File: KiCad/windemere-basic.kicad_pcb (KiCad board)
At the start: 2 copper layers, 146.1 x 157.5 mm, 57 parts, among them J1 Barrel_Jack, SW1 Push_Button, SW2 SW_SPDT, U1 HD44780U, U2 WD65C02, U3 28C256, U4 62256, U5 WD65C22, U6 74HC00, U7 MM74C922, U8 L7805, X1 1MHz

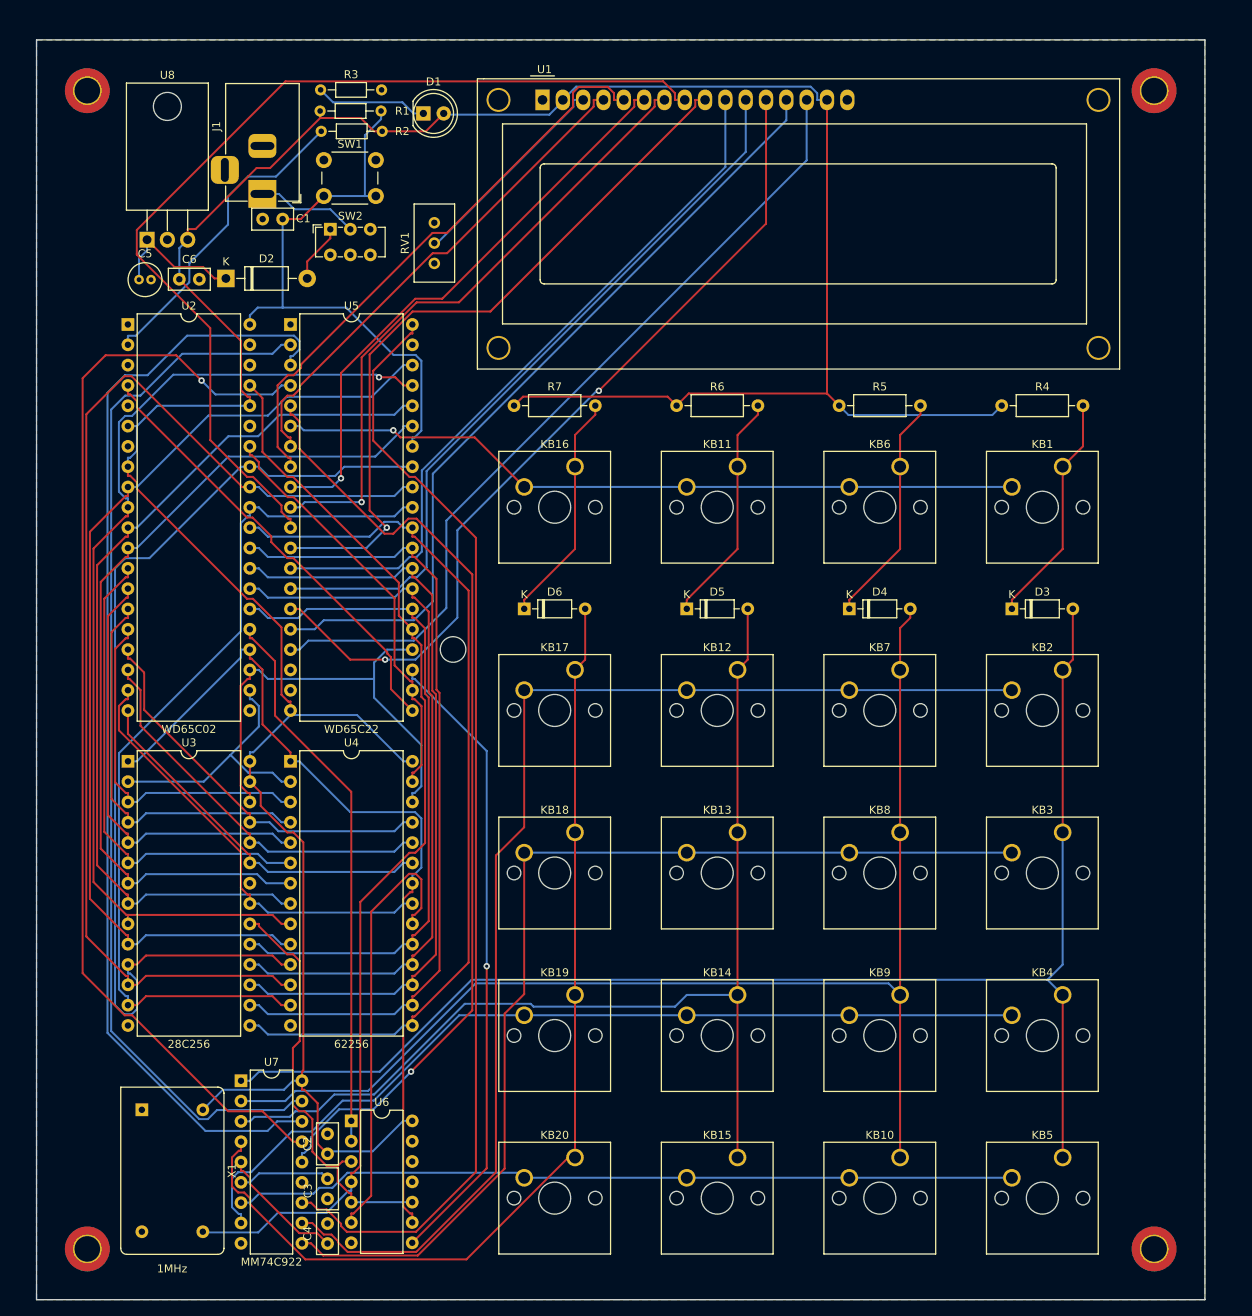
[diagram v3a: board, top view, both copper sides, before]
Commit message: Add J1
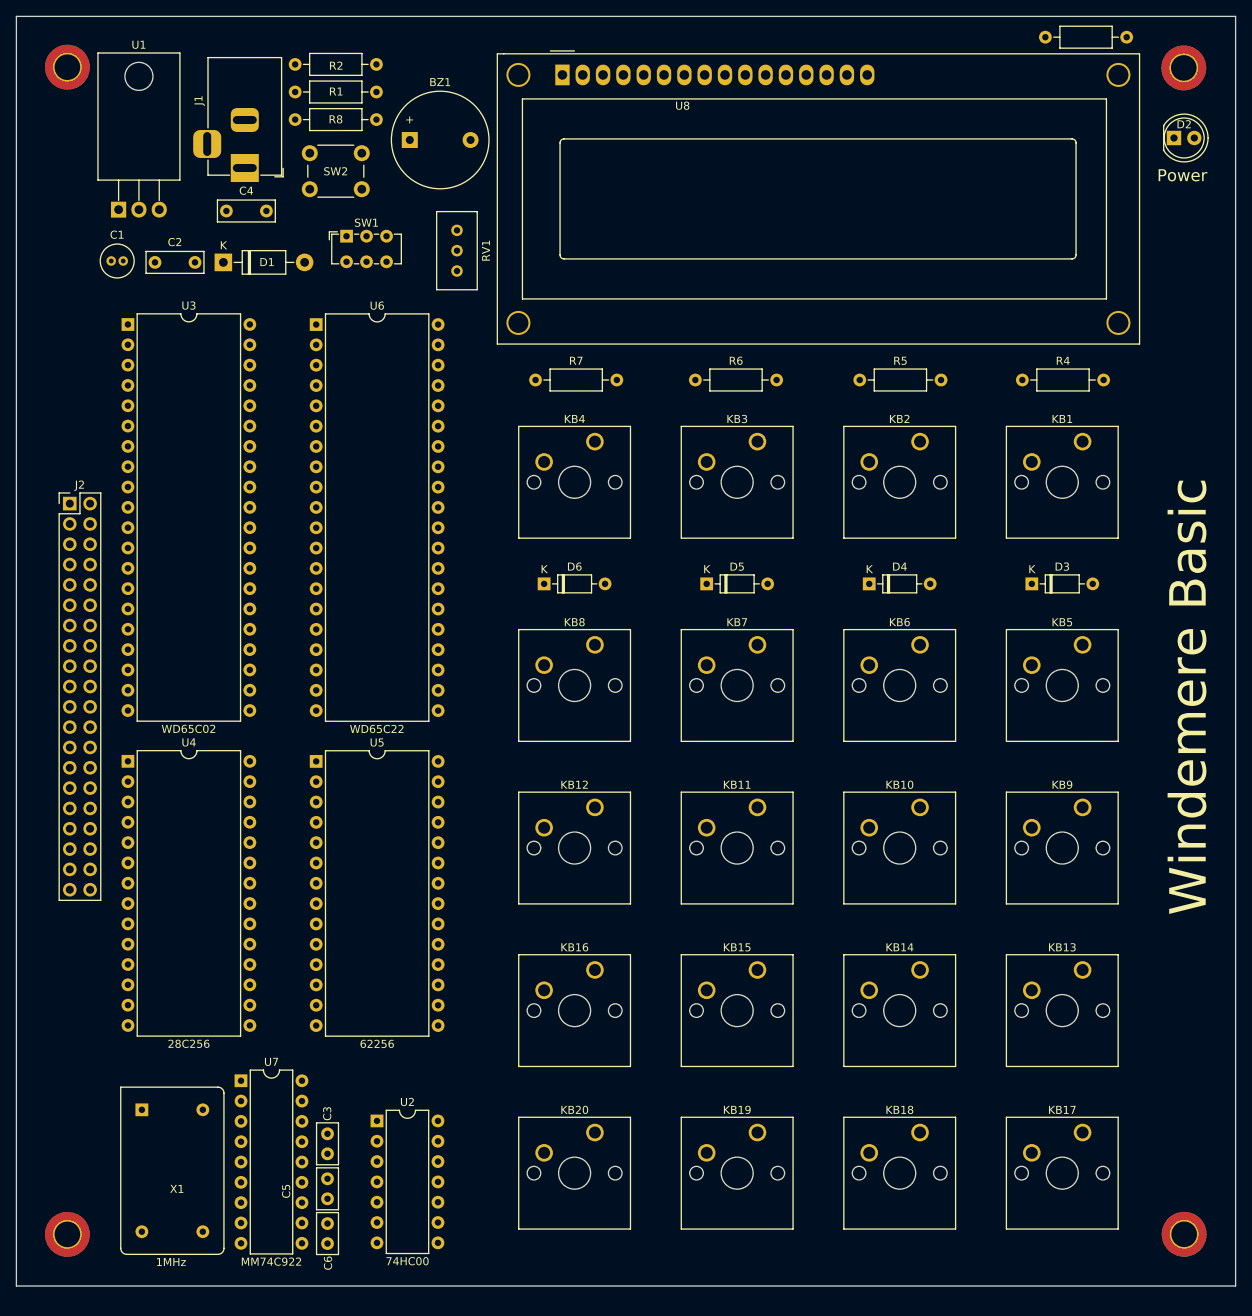
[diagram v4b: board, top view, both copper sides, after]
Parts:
- removed the R7 at (195.6, 81.3)
- removed REF?: MountingHole_3.2mm_M3, MountingHole:MountingHole_3.2mm_M3
- removed the U1 at (199.1, 43.1)
- added BZ1: Buzzer, Buzzer_Beeper:Buzzer_12x9.5RM7.6, F.Cu at (182.6, 48.1)
- added J2: Conn_02x20, Connector_PinHeader_2.54mm:PinHeader_2x20_P2.54mm_Vertical, F.Cu at (140.1, 93.5)
- added R3: 1k, Resistor_THT:R_Axial_DIN0207_L6.3mm_D2.5mm_P10.16mm_Horizontal, F.Cu at (262.0, 35.2)
- added R8: 1K, Resistor_THT:R_Axial_DIN0207_L6.3mm_D2.5mm_P10.16mm_Horizontal, F.Cu at (168.2, 45.5)
- added REF**: OSHW-Logo_11.4x12mm_SilkScreen, Symbol:OSHW-Logo_11.4x12mm_SilkScreen, B.Cu at (208.0, 65.2)
- added U8: HD44780U, Display:WC1602A, F.Cu at (201.6, 39.9)
- added memory_map: 6502-Memory_Map, memory_map:6502-Memory_Map, F.Cu at (236.0, 65.3)
- C2: renamed from C6; footprint Capacitor_THT:C_Disc_D5.0mm_W2.5mm_P2.50mm -> Capacitor_THT:C_Disc_D7.0mm_W2.5mm_P5.00mm
- C4: renamed from C1; footprint Capacitor_THT:C_Disc_D5.0mm_W2.5mm_P2.50mm -> Capacitor_THT:C_Disc_D7.0mm_W2.5mm_P5.00mm
- R1: renamed from R2; footprint Resistor_THT:R_Axial_DIN0204_L3.6mm_D1.6mm_P7.62mm_Horizontal -> Resistor_THT:R_Axial_DIN0207_L6.3mm_D2.5mm_P10.16mm_Horizontal
- R2: renamed from R3; value 1k -> 1K; footprint Resistor_THT:R_Axial_DIN0204_L3.6mm_D1.6mm_P7.62mm_Horizontal -> Resistor_THT:R_Axial_DIN0207_L6.3mm_D2.5mm_P10.16mm_Horizontal
- R7: renamed from R1; value 1K -> 100K; footprint Resistor_THT:R_Axial_DIN0204_L3.6mm_D1.6mm_P7.62mm_Horizontal -> Resistor_THT:R_Axial_DIN0207_L6.3mm_D2.5mm_P10.16mm_Horizontal
- SW2: renamed from SW1; value Push_Button -> Push_Button_small
- moved D2 93.9 mm to (278.1, 47.8)
- moved KB4 90.6 mm to (205.7, 85.8)
- moved KB17 85.9 mm to (266.6, 172.1)
- moved KB5 64.1 mm to (266.6, 111.2)
- moved KB16 63.0 mm to (205.7, 151.8)
- moved KB3 62.0 mm to (226.0, 85.8)
- moved KB18 57.2 mm to (246.3, 172.1)
- moved KB13 46.4 mm to (266.6, 151.8)
- moved KB8 44.8 mm to (205.7, 111.2)
- moved KB10 43.8 mm to (246.3, 131.5)
- moved R7 43.1 mm to (198.3, 78.1)
- moved KB11 42.7 mm to (226.0, 131.5)
- moved KB2 33.6 mm to (246.3, 85.8)
- moved KB9 32.7 mm to (266.6, 131.5)
- moved KB19 28.6 mm to (226.0, 172.1)
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- renumbered C5 to C1, C2 to C3, C3 to C5, C4 to C6, D2 to D1, D1 to D2, SW2 to SW1, U8 to U1, U6 to U2, U2 to U3, U3 to U4, U4 to U5, U5 to U6
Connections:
- C4 pad 1: Net-(C1-Pad1) (its old number) -> Net-(C4-Pad1)
- D2 pad 1: Net-(D1-Pad1) -> Net-(D2-Pad1)
- KB11 pad 1: Net-(D5-Pad1) -> Net-(D5-Pad2)
- KB11 pad 2: Net-(KB1-Pad2) -> Net-(KB10-Pad2)
- KB12 pad 1: Net-(D5-Pad2) -> Net-(D6-Pad2)
- KB12 pad 2: Net-(KB12-Pad2) -> Net-(KB10-Pad2)
- KB13 pad 1: Net-(D5-Pad2) -> Net-(D3-Pad2)
- KB14 pad 1: Net-(D5-Pad2) -> Net-(D4-Pad2)
- KB14 pad 2: Net-(KB14-Pad2) -> Net-(KB13-Pad2)
- KB15 pad 2: Net-(KB10-Pad2) -> Net-(KB13-Pad2)
- KB16 pad 1: Net-(D6-Pad1) -> Net-(D6-Pad2)
- KB16 pad 2: Net-(KB1-Pad2) -> Net-(KB13-Pad2)
- KB17 pad 1: Net-(D6-Pad2) -> Net-(D3-Pad2)
- KB17 pad 2: Net-(KB12-Pad2) -> Net-(KB17-Pad2)
- KB18 pad 1: Net-(D6-Pad2) -> Net-(D4-Pad2)
- KB18 pad 2: Net-(KB13-Pad2) -> Net-(KB17-Pad2)
- KB19 pad 1: Net-(D6-Pad2) -> Net-(D5-Pad2)
- KB19 pad 2: Net-(KB14-Pad2) -> Net-(KB17-Pad2)
- KB2 pad 1: Net-(D3-Pad2) -> Net-(D4-Pad1)
- KB2 pad 2: Net-(KB12-Pad2) -> Net-(KB1-Pad2)
- KB20 pad 2: Net-(KB10-Pad2) -> Net-(KB17-Pad2)
- KB3 pad 1: Net-(D3-Pad2) -> Net-(D5-Pad1)
- KB3 pad 2: Net-(KB13-Pad2) -> Net-(KB1-Pad2)
- KB4 pad 1: Net-(D3-Pad2) -> Net-(D6-Pad1)
- KB4 pad 2: Net-(KB14-Pad2) -> Net-(KB1-Pad2)
- KB5 pad 2: Net-(KB10-Pad2) -> Net-(KB5-Pad2)
- KB6 pad 1: Net-(D4-Pad1) -> Net-(D4-Pad2)
- KB6 pad 2: Net-(KB1-Pad2) -> Net-(KB5-Pad2)
- KB7 pad 1: Net-(D4-Pad2) -> Net-(D5-Pad2)
- KB7 pad 2: Net-(KB12-Pad2) -> Net-(KB5-Pad2)
- KB8 pad 1: Net-(D4-Pad2) -> Net-(D6-Pad2)
- KB8 pad 2: Net-(KB13-Pad2) -> Net-(KB5-Pad2)
- KB9 pad 1: Net-(D4-Pad2) -> Net-(D3-Pad2)
- KB9 pad 2: Net-(KB14-Pad2) -> Net-(KB10-Pad2)
- R2 pad 1: Net-(D1-Pad1) -> Net-(J2-Pad34)
- R2 pad 2: GND -> +5V
- R7 pad 2: Net-(C1-Pad1) (its old number) -> Net-(D6-Pad1)
- SW2 pad 2: Net-(C1-Pad1) (its old number) -> Net-(C4-Pad1)
- U3 pad 40: Net-(C1-Pad1) (its old number) -> Net-(C4-Pad1)
- U3 pad 6: +5V -> Net-(J2-Pad34)
- U6 pad 19: unconnected-(U5-Pad19) -> Net-(BZ1-Pad1)
- U6 pad 34: Net-(C1-Pad1) (its old number) -> Net-(C4-Pad1)
- U7 pad 10: Net-(KB13-Pad2) -> Net-(KB10-Pad2)
- U7 pad 11: Net-(KB12-Pad2) -> Net-(KB5-Pad2)
- U7 pad 7: Net-(KB10-Pad2) -> Net-(KB17-Pad2)
- U7 pad 8: Net-(KB14-Pad2) -> Net-(KB13-Pad2)
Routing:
- net +5V: track 386.1 -> 0.00 mm
- net Net-(D3-Pad2): track 176.7 -> 0.00 mm
- net Net-(D4-Pad2): track 158.2 -> 0.00 mm
- net Net-(KB12-Pad2): track 152.6 -> 0.00 mm
- net /D1: track 144.4 -> 0.00 mm
- net Net-(U6-Pad3): track 140.8 -> 0.00 mm
- net Net-(U6-Pad40): track 140.3 -> 0.00 mm
- net Net-(U6-Pad4): track 140.2 -> 0.00 mm, vias 1 -> 0
- net Net-(D5-Pad2): track 138.0 -> 0.00 mm
- net Net-(J2-Pad28): track 135.5 -> 0.00 mm
- net Net-(U6-Pad2): track 132.8 -> 0.00 mm
- net Net-(KB13-Pad2): track 131.9 -> 0.00 mm
- net /D0: track 128.9 -> 0.00 mm
- net Net-(D6-Pad2): track 128.5 -> 0.00 mm
- net /A1: track 127.7 -> 0.00 mm, vias 1 -> 0
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- removed copper zone on B.Cu, net GND
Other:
- board size 146.1 x 157.5 mm -> 152.4 x 158.7 mm
- board text added: "Power"
- board text added: "Windemere Basic"
- board text added: "©2022 by Matt Rude <matt@mattrude.com>"
- board text added: "©2022 by Matt Rude <matt@mattrude.com> https://github.com/mattrude/windemere-basic"

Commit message: Added MCP102-475 to reset line
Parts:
- removed REF**: OSHW-Logo_11.4x12mm_SilkScreen, Symbol:OSHW-Logo_11.4x12mm_SilkScreen
- added U9: MCP102-475, Package_TO_SOT_THT:TO-92, F.Cu at (139.8, 73.5)
- J2: value Conn_02x20 -> Connector

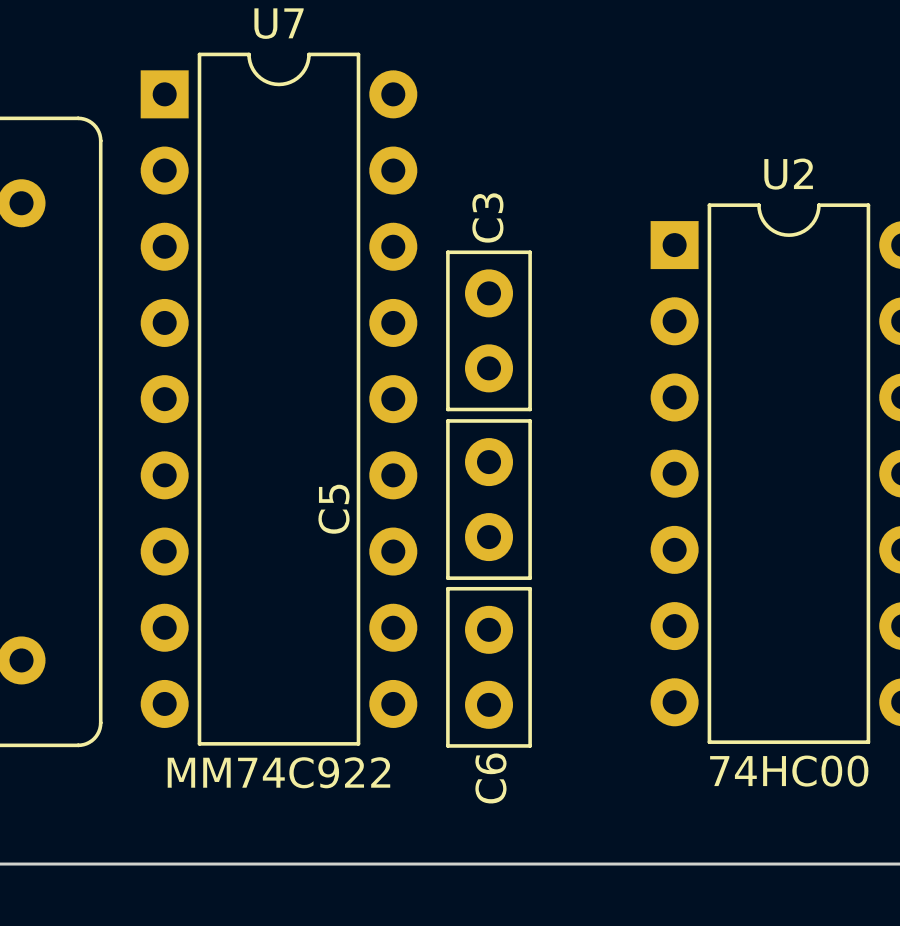
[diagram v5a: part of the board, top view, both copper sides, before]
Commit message: Add Digikey Part Numbers
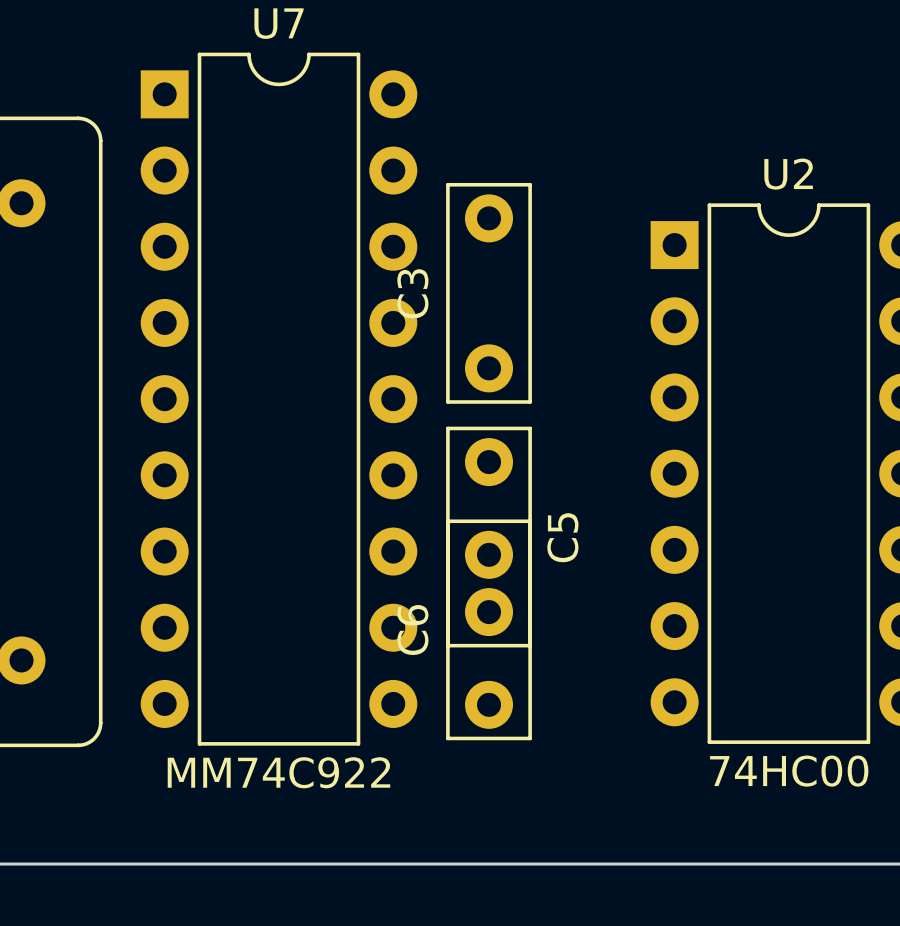
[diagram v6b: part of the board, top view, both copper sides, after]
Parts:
- C2: value 0.1µF -> 0.1uF
- C3, C5, C6: footprint Capacitor_THT:C_Disc_D5.0mm_W2.5mm_P2.50mm -> Capacitor_THT:C_Disc_D7.0mm_W2.5mm_P5.00mm
- R3: value 1k -> 1K
- SW2: value Push_Button_small -> Push_Button

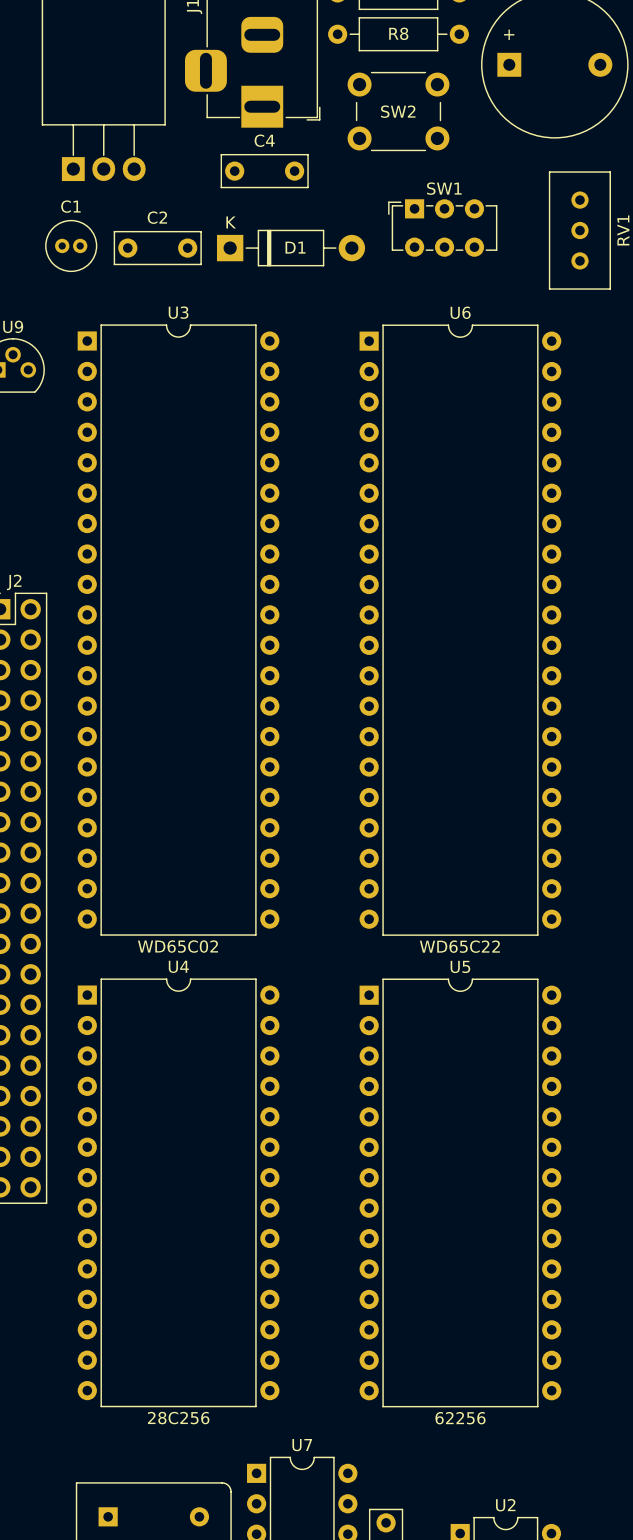
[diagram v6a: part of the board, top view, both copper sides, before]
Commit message: Add Zif socket to eprom
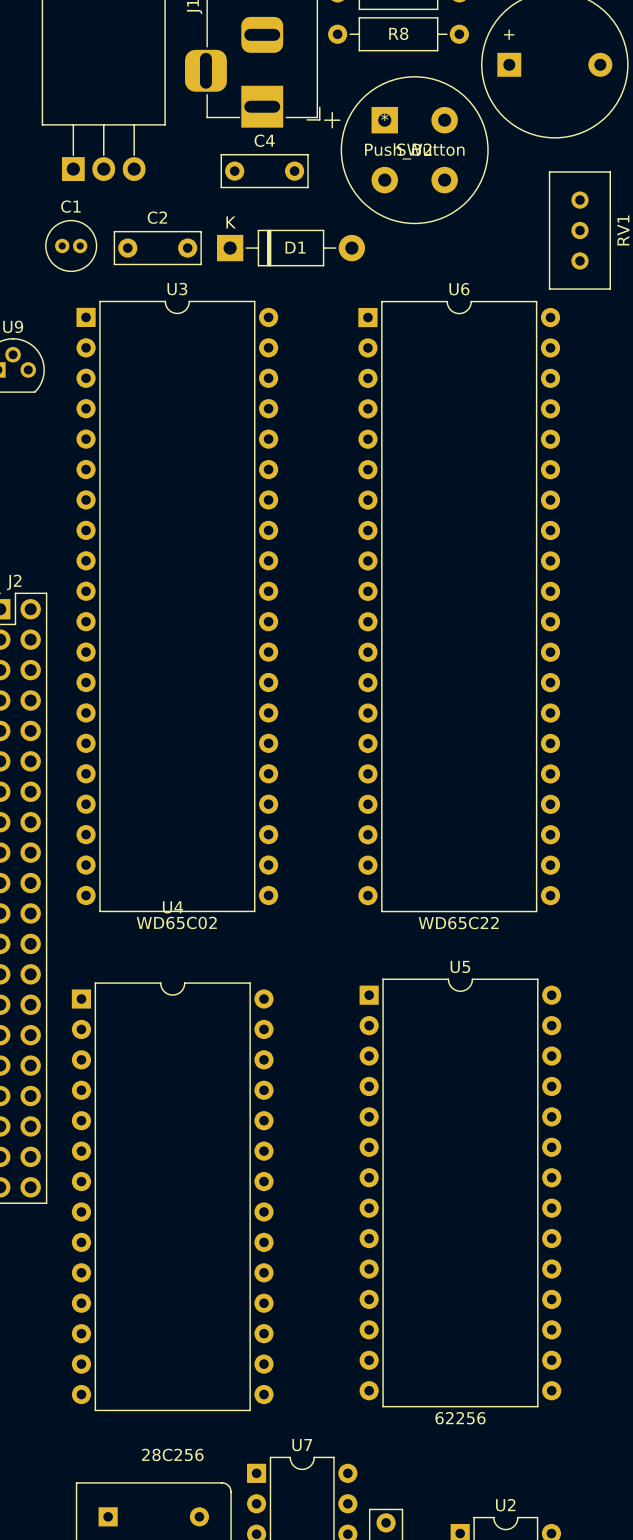
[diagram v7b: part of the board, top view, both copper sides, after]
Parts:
- removed SW1: SW_SPDT, Button_Switch_THT:SW_E-Switch_EG1271_DPDT
- D2: value LED -> LED_Red
- SW2: footprint Button_Switch_THT:SW_PUSH_6mm -> footprints:D6R90F1LFS
- U4: footprint Package_DIP:DIP-28_W15.24mm -> Package_DIP:DIP-28_W15.24mm-ziff
- moved U4 4.78 mm to (146.8, 121.0)
- moved SW2 3.64 mm to (172.2, 52.7)
- moved U3 1.97 mm to (147.2, 69.2)
- moved U6 1.97 mm to (170.8, 69.2)

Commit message: update socket
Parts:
- added SW1: SW_SPDT, Button_Switch_THT:SW_E-Switch_EG1271_DPDT, F.Cu at (284.2, 31.6)
- SW2: value Push_Button -> Reset Button
- U4: footprint Package_DIP:DIP-28_W15.24mm-ziff -> sockets:eeprom_socket
- moved D1 16.8 mm to (168.2, 49.1)
- moved C1 9.29 mm to (154.2, 61.0)
- moved C2 8.29 mm to (158.5, 60.5)
- moved BZ1 4.59 mm to (182.2, 43.5)
- moved RV1 4.40 mm to (188.4, 60.0)
- moved C3 4.08 mm to (173.7, 171.0)
- moved SW2 3.67 mm to (171.2, 56.2)
- moved U5 2.30 mm to (170.4, 128.0)
- moved C5 1.61 mm to (173.7, 178.8), turned to 90 degrees
- moved C6 1.48 mm to (173.7, 186.5)
- moved U4 1.41 mm to (145.4, 121.0)
- moved C4 1.34 mm to (158.5, 56.3)
- moved J2 1.13 mm to (138.9, 93.5)
- moved X1 0.53 mm to (149.1, 169.8)
- moved U7 0.53 mm to (161.4, 166.2)
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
